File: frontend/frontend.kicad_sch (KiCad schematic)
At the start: 54 parts, among them Q1 T2N7002AK,LM, Q2 NX3008PBK,215, Q3 NX3008PBK,215, Q4 T2N7002AK,LM, Q5 NX3008PBK,215, Q6 T2N7002AK,LM, U1 ADS1291/2, U2 KC2016Z2

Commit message: Allow reading back CLKSEL
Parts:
- removed R15: 1M, Resistor_SMD:R_0603_1608Metric, symbol Device:R
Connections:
- net at JP1.2 (C), U1.14 (CLKSEL): now also U1.25 (GPIO2/RCLK2)
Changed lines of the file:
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@@
   (junction (at 156.21 80.01) (diameter 0) (color 0 0 0 0)
   )
+  (junction (at 180.34 132.08) (diameter 0) (color 0 0 0 0)
+  )
   (junction (at 24.13 93.98) (diameter 0) (color 0 0 0 0)
   )
@@
     (stroke (width 0) (type default))
   )
-  (wire (pts (xy 175.26 111.76) (xy 172.72 111.76))
-    (stroke (width 0) (type default))
-  )
   (wire (pts (xy 121.92 116.84) (xy 121.92 114.3))
     (stroke (width 0) (type default))
@@
     (stroke (width 0) (type default))
   )
+  (wire (pts (xy 180.34 132.08) (xy 203.2 132.08))
+    (stroke (width 0) (type default))
+  )
   (wire (pts (xy 161.29 116.84) (xy 190.5 116.84))
     (stroke (width 0) (type default))
@@
     (stroke (width 0) (type default))
   )
+  (wire (pts (xy 180.34 111.76) (xy 180.34 132.08))
+    (stroke (width 0) (type default))
+  )
   (wire (pts (xy 114.3 132.08) (xy 114.3 134.62))
     (stroke (width 0) (type default))
@@
     (stroke (width 0) (type default))
   )
-  (wire (pts (xy 165.1 111.76) (xy 161.29 111.76))
+  (wire (pts (xy 161.29 111.76) (xy 180.34 111.76))
     (stroke (width 0) (type default))
   )
@@
     (stroke (width 0) (type default))
   )
-  (wire (pts (xy 175.26 113.03) (xy 175.26 111.76))
-    (stroke (width 0) (type default))
-  )
   (wire (pts (xy 99.06 99.06) (xy 125.73 99.06))
     (stroke (width 0) (type default))
@@
     (stroke (width 0) (type default))
   )
-  (wire (pts (xy 161.29 132.08) (xy 203.2 132.08))
+  (wire (pts (xy 161.29 132.08) (xy 180.34 132.08))
     (stroke (width 0) (type default))
   )
@@
         (path "/e7afbd42-f5d0-401b-b125-21ade79cd152"
           (reference "C12") (unit 1)
-        )
-      )
-    )
-  )
-  (symbol (lib_id "power:GND") (at 175.26 113.03 0) (unit 1)
-    (in_bom yes) (on_board yes) (dnp no)
-    (property "Reference" "#PWR022" (at 175.26 119.38 0)
-      (effects (font (size 1.27 1.27)) hide)
-    )
-    (property "Value" "GND" (at 179.07 113.03 0)
-      (effects (font (size 1.27 1.27)))
-    )
-    (property "Footprint" "" (at 175.26 113.03 0)
-      (effects (font (size 1.27 1.27)) hide)
-    )
-    (property "Datasheet" "" (at 175.26 113.03 0)
-      (effects (font (size 1.27 1.27)) hide)
-    )
-    (pin "1")
-    (instances
-      (project "frontend"
-        (path "/e7afbd42-f5d0-401b-b125-21ade79cd152"
-          (reference "#PWR022") (unit 1)
         )
       )
@@
         )
       )
-    )
-  )
-  (symbol (lib_id "Device:R") (at 168.91 111.76 270) (unit 1)
-    (in_bom yes) (on_board yes) (dnp no)
-    (property "Reference" "R15" (at 166.37 114.3 90)
-      (effects (font (size 1.27 1.27)))
-    )
-    (property "Value" "1M" (at 170.18 114.3 90)
-      (effects (font (size 1.27 1.27)))
-    )
-    (property "Footprint" "Resistor_SMD:R_0603_1608Metric" (at 168.91 109.982 90)
-      (effects (font (size 1.27 1.27)) hide)
-    )
-    (property "Datasheet" "~" (at 168.91 111.76 0)
-      (effects (font (size 1.27 1.27)) hide)
-    )
-    (pin "1")
-    (pin "2")
-    (instances
-      (project "frontend"
-        (path "/e7afbd42-f5d0-401b-b125-21ade79cd152"
-          (reference "R15") (unit 1)
-        )
-      )

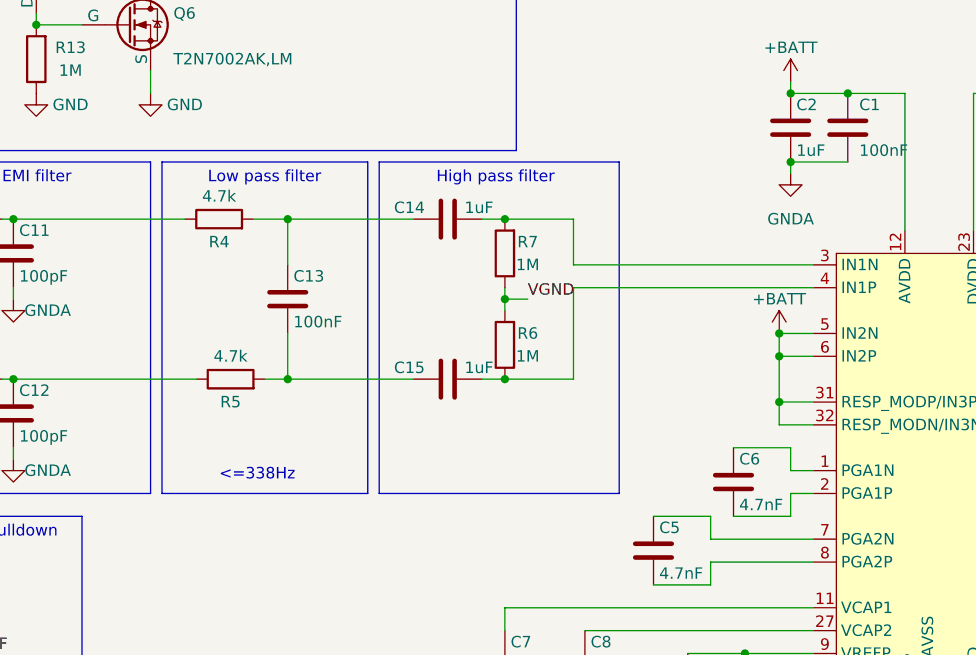
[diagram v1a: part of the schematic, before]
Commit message: Fix #11: remove filters
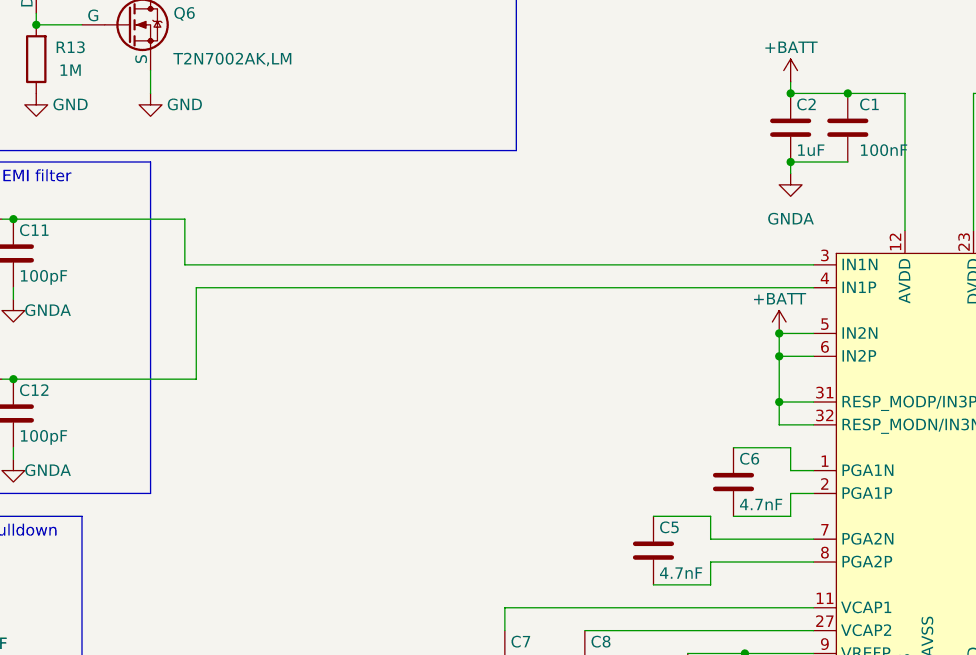
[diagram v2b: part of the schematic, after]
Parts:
- removed C13: 100nF, Capacitor_SMD:C_0603_1608Metric, symbol Device:C
- removed C14, C15: 1uF, Capacitor_SMD:C_0603_1608Metric, symbol Device:C
- removed R4, R5: 4.7k, Resistor_SMD:R_0603_1608Metric, symbol Device:R
- removed R6, R7: 1M, Resistor_SMD:R_0603_1608Metric, symbol Device:R
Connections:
- net at C12.1, R2.2: now also U1.4 (IN1P)
- net at C11.1, R1.2: now also U1.3 (IN1N)
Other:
- note removed: "<=338Hz"
- note removed: "High pass filter"
- note removed: "Low pass filter"

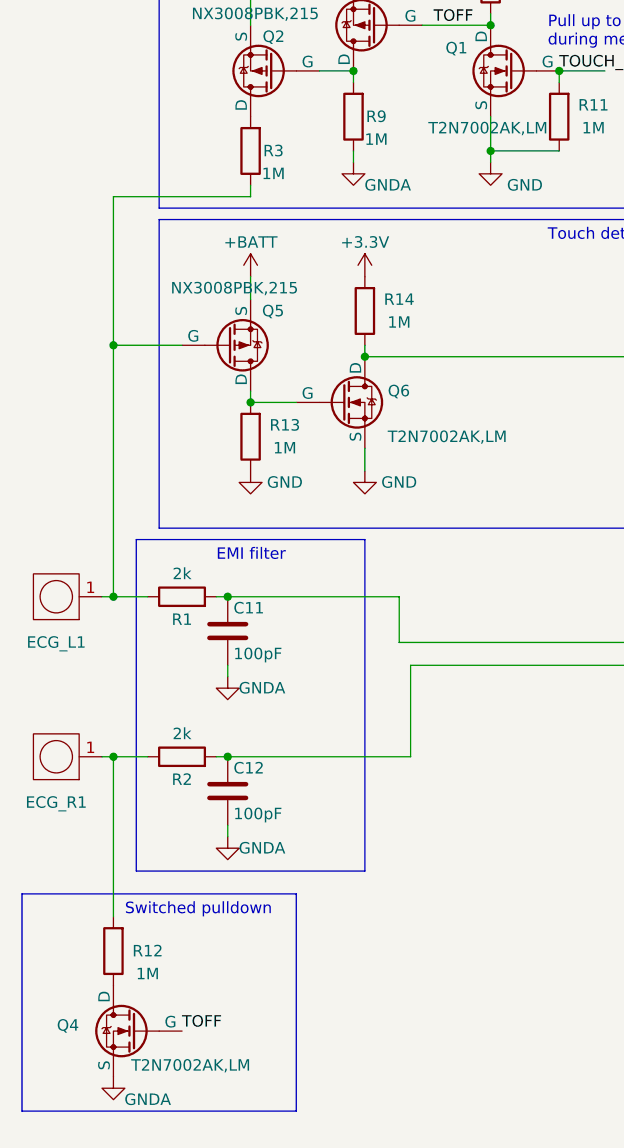
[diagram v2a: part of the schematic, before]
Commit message: Fix #5: tune touch detector resistors
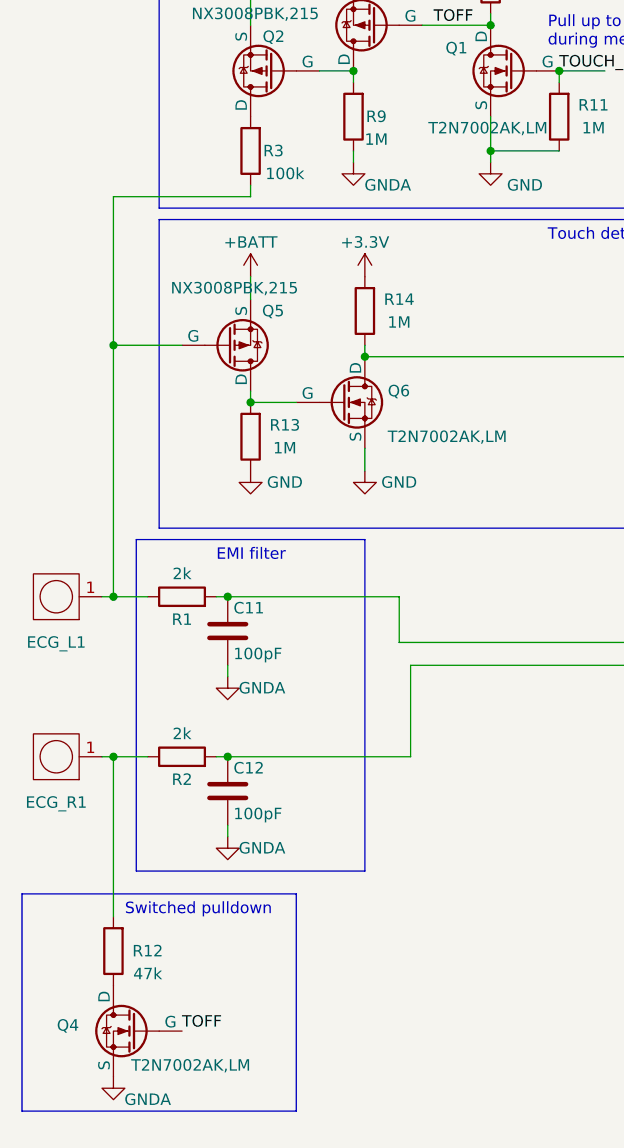
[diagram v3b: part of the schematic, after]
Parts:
- R12: value 1M -> 47k
- R3: value 1M -> 100k
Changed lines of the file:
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@@
       (effects (font (size 1.27 1.27)))
     )
-    (property "Value" "1M" (at 41.91 46.99 0)
+    (property "Value" "100k" (at 43.18 46.99 0)
       (effects (font (size 1.27 1.27)))
     )
@@
       (effects (font (size 1.27 1.27)))
     )
-    (property "Value" "1M" (at 27.94 135.89 0)
-      (effects (font (size 1.27 1.27)))
-    )
+    (property "Value" "47k" (at 27.94 135.89 0)
+      (effects (font (size 1.27 1.27)))
+    )
